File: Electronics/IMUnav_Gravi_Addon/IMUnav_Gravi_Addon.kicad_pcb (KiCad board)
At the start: 2 copper layers, 1 part, among them U1 hw-045

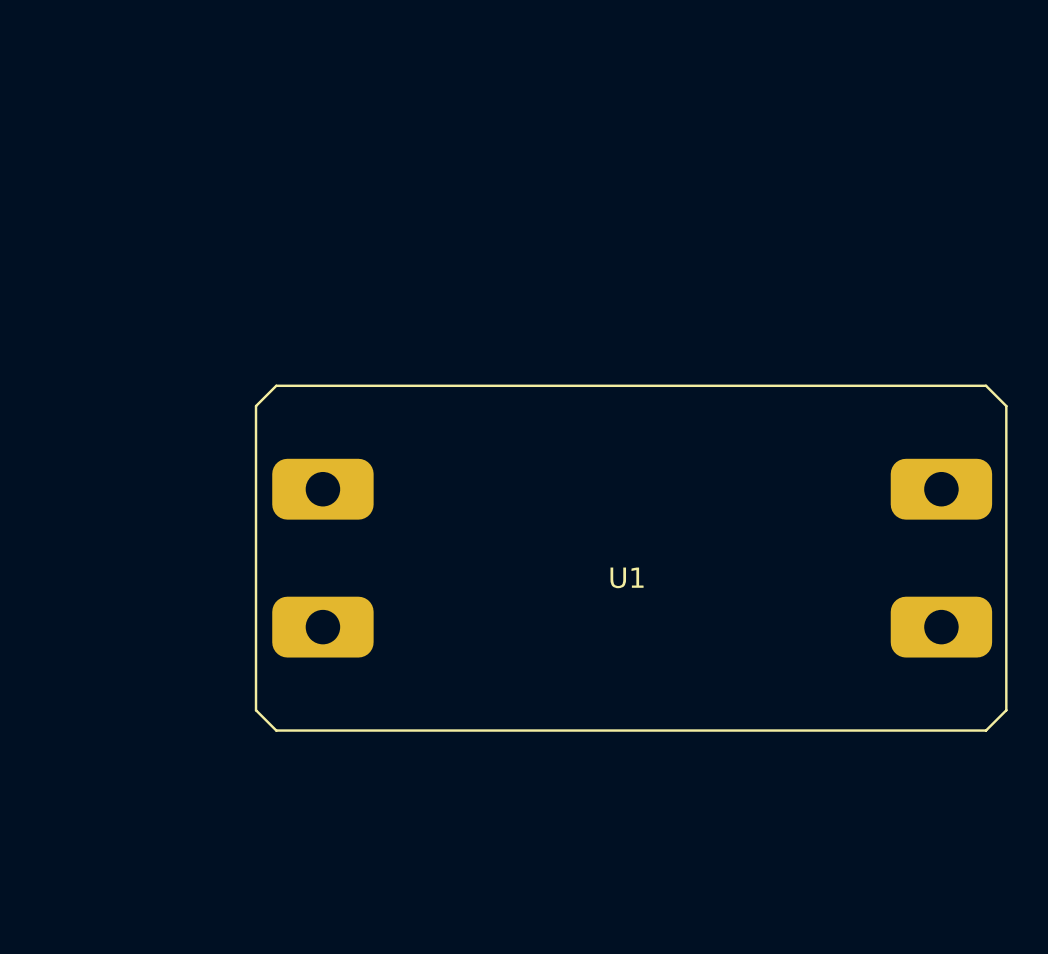
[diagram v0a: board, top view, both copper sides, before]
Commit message: addon pcb, added 3d models
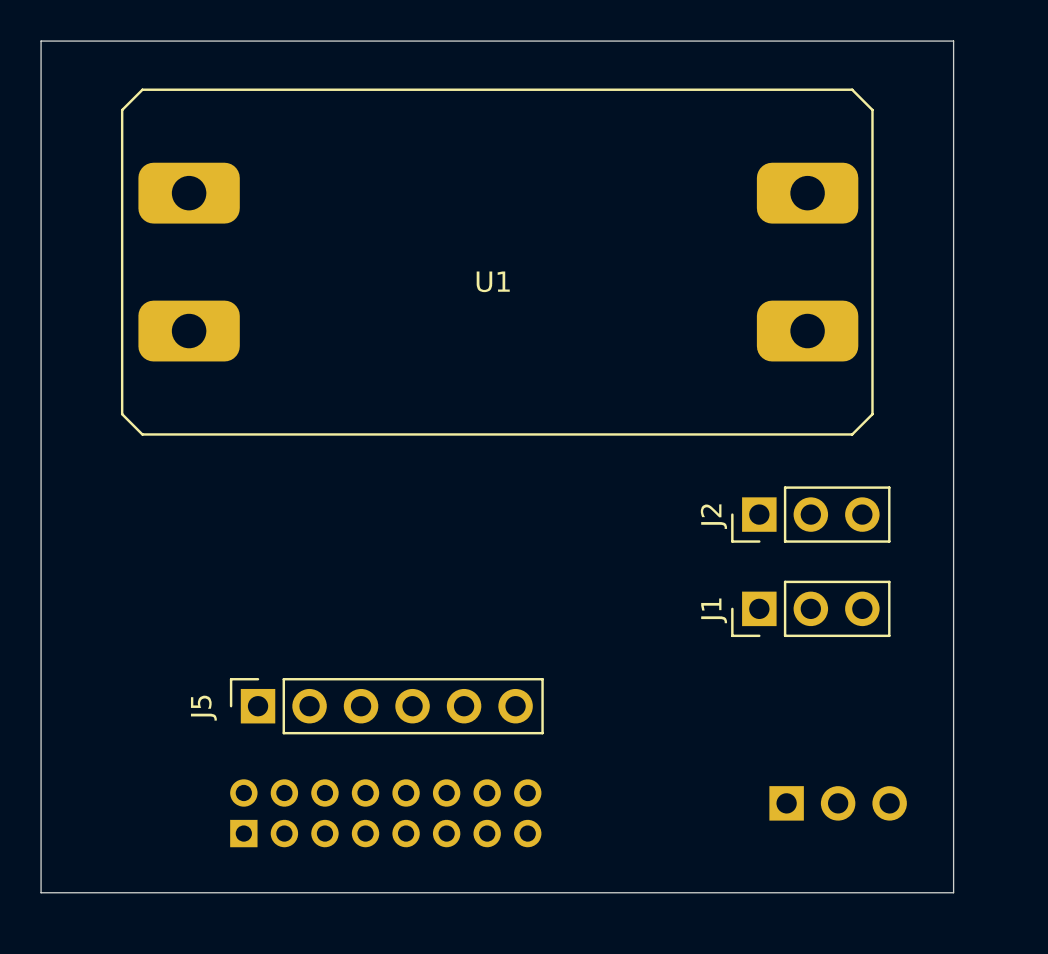
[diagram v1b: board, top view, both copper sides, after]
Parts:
- added J1: Conn_01x03_Pin, Connector_PinHeader_2.54mm:PinHeader_1x03_P2.54mm_Vertical, F.Cu at (35.4, 28.0)
- added J2: Conn_01x03_Pin, Connector_PinHeader_2.54mm:PinHeader_1x03_P2.54mm_Vertical, F.Cu at (35.4, 23.4)
- added J3: Conn_02x08_Odd_Even, Connector_PinSocket_2.00mm:PinSocket_2x08_P2.00mm_Vertical, B.Cu at (10.0, 39.1)
- added J4: Conn_01x03_Socket, Connector_PinSocket_2.54mm:PinSocket_1x03_P2.54mm_Vertical, B.Cu at (36.8, 37.6)
- added J5: BMP280-module, Connector_PinSocket_2.54mm:PinSocket_1x06_P2.54mm_Vertical, F.Cu at (10.7, 32.8)
- U1: value hw-045 -> MT3608-module
- moved U1 16.0 mm to (22.3, 11.4)
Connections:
- U1 pad 1: unconnected-(U1-VIN+-Pad1) -> +3V3
- U1 pad 2: unconnected-(U1-VIN--Pad2) -> GND
- U1 pad 3: unconnected-(U1-VOUT--Pad3) -> GND
- U1 pad 4: unconnected-(U1-VOUT--Pad4) -> Vdrive
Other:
- board outline added: 45 x 42 mm

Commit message: addon pcb routing
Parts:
- added H1: MountingHole, MountingHole:MountingHole_3.2mm_M3, F.Cu at (4.00, 36.0)
- added H2: MountingHole, MountingHole:MountingHole_3.2mm_M3, F.Cu at (5.50, 4.50)
- added JP1: SolderJumper_3_Bridged12, Jumper:SolderJumper-3_P1.3mm_Bridged12_RoundedPad1.0x1.5mm_NumberLabels, B.Cu at (43.3, 27.1)
- added JP2: SolderJumper_3_Bridged12, Jumper:SolderJumper-3_P1.3mm_Bridged12_RoundedPad1.0x1.5mm_NumberLabels, B.Cu at (40.1, 27.1)
- moved J5 20.2 mm to (30.9, 33.6)
- moved J2 18.5 mm to (19.1, 32.0), turned to -90 degrees
- moved J1 16.3 mm to (19.1, 27.7), turned to -90 degrees
- moved U1 5.41 mm to (27.1, 13.9)
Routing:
- net Vdrive: track 0.00 -> 35.8 mm
- net SCL: track 0.00 -> 12.8 mm
- net SERVO1: track 0.00 -> 11.5 mm
- net CSB: track 0.00 -> 10.0 mm
- net SDO: track 0.00 -> 8.36 mm
- net SERVO2: track 0.00 -> 5.08 mm
- net +3V3: track 0.00 -> 4.90 mm, vias 0 -> 1
- net SDA: track 0.00 -> 4.70 mm
- added copper zone on F.Cu, net +3V3
- added copper zone on B.Cu, net GND
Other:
- board size 45 x 42 mm -> 46 x 43 mm

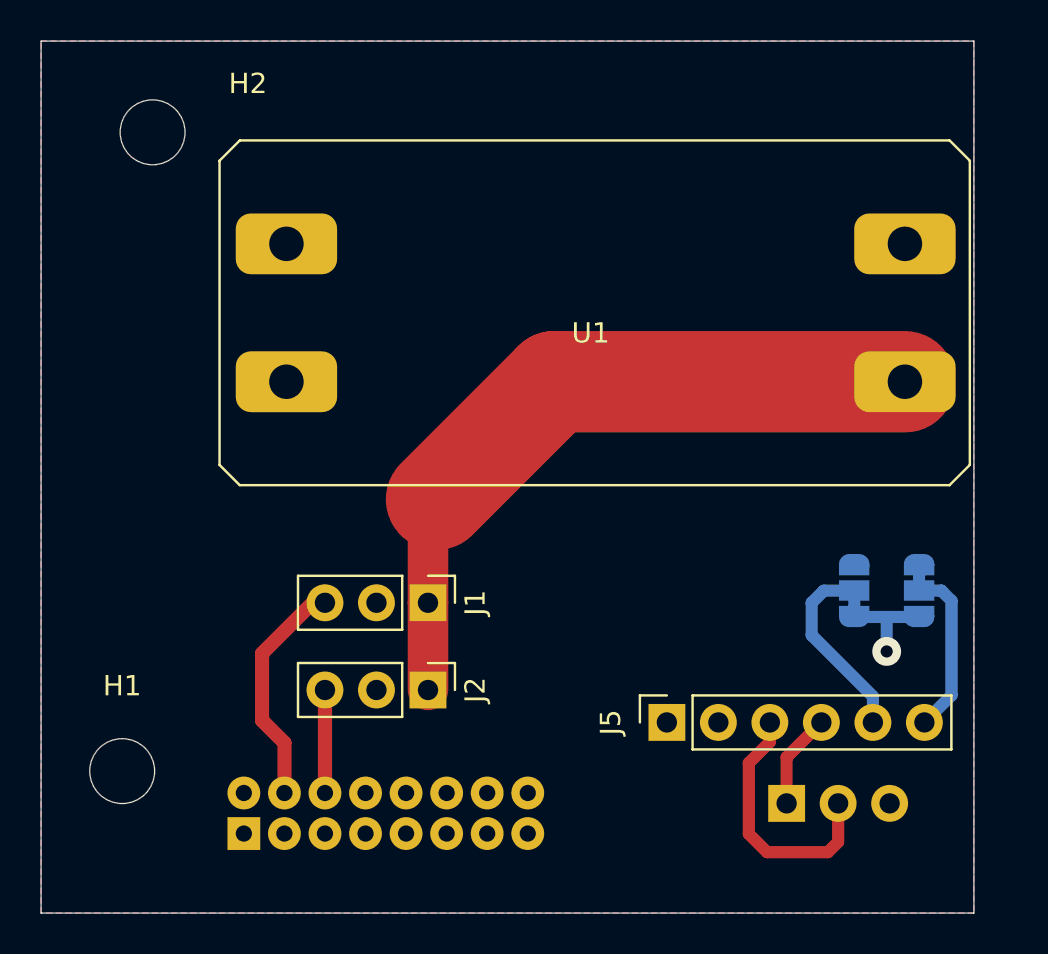
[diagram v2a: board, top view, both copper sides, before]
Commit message: update for manufacturability with npth vias
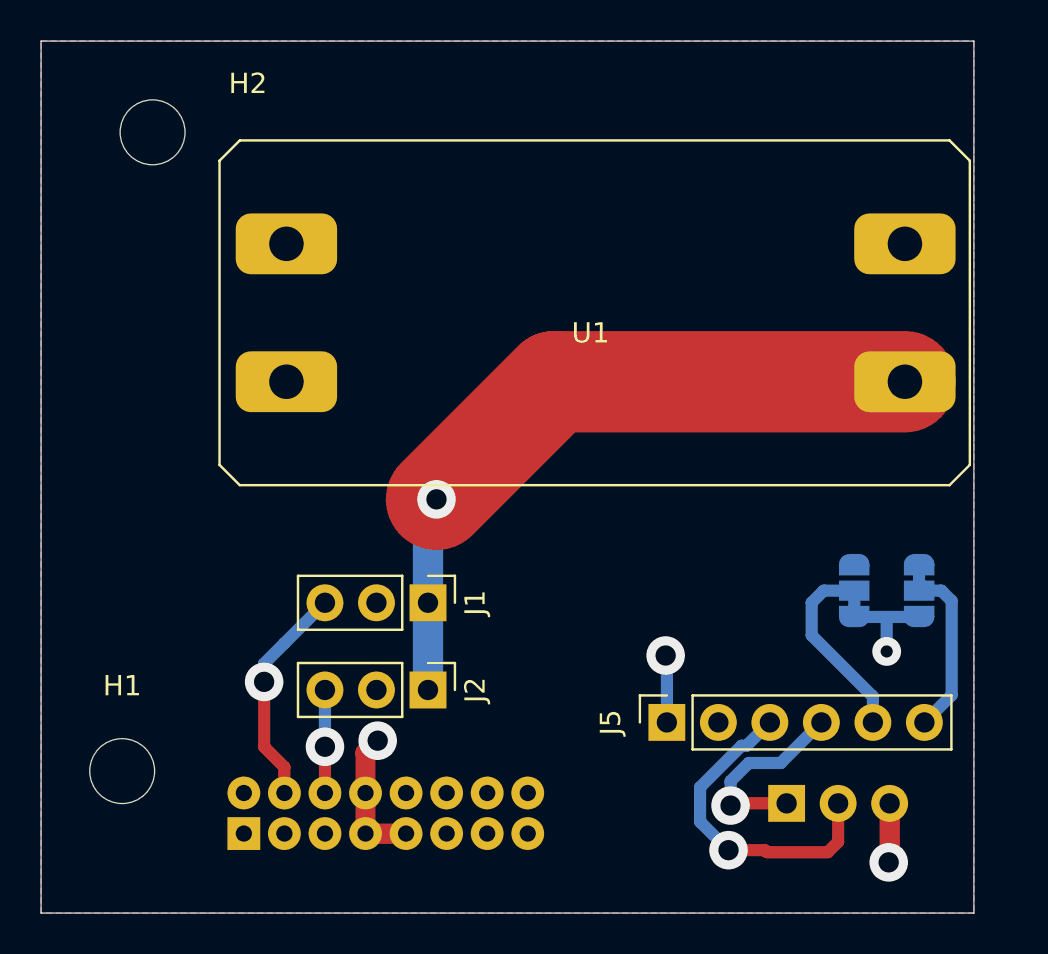
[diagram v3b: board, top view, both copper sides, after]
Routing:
- net GND: track 0.00 -> 9.76 mm, vias 0 -> 2
- net SDA: track 4.70 -> 9.69 mm, vias 0 -> 1
- net +3V3: track 4.90 -> 8.31 mm, vias 1 -> 2
- net SCL: track 12.8 -> 16.0 mm, vias 0 -> 1
- net Vdrive: track 35.8 -> 36.4 mm, vias 0 -> 1
- net SERVO1: track 11.5 -> 11.1 mm, vias 0 -> 1
- net SERVO2: vias 0 -> 1
